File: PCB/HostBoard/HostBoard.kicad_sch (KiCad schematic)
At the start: 8 parts, among them J1 Conn_01x06, J2 Conn_01x06, J3 Conn_01x06, U1 MCP23017_SS, U2 TB6612FNG

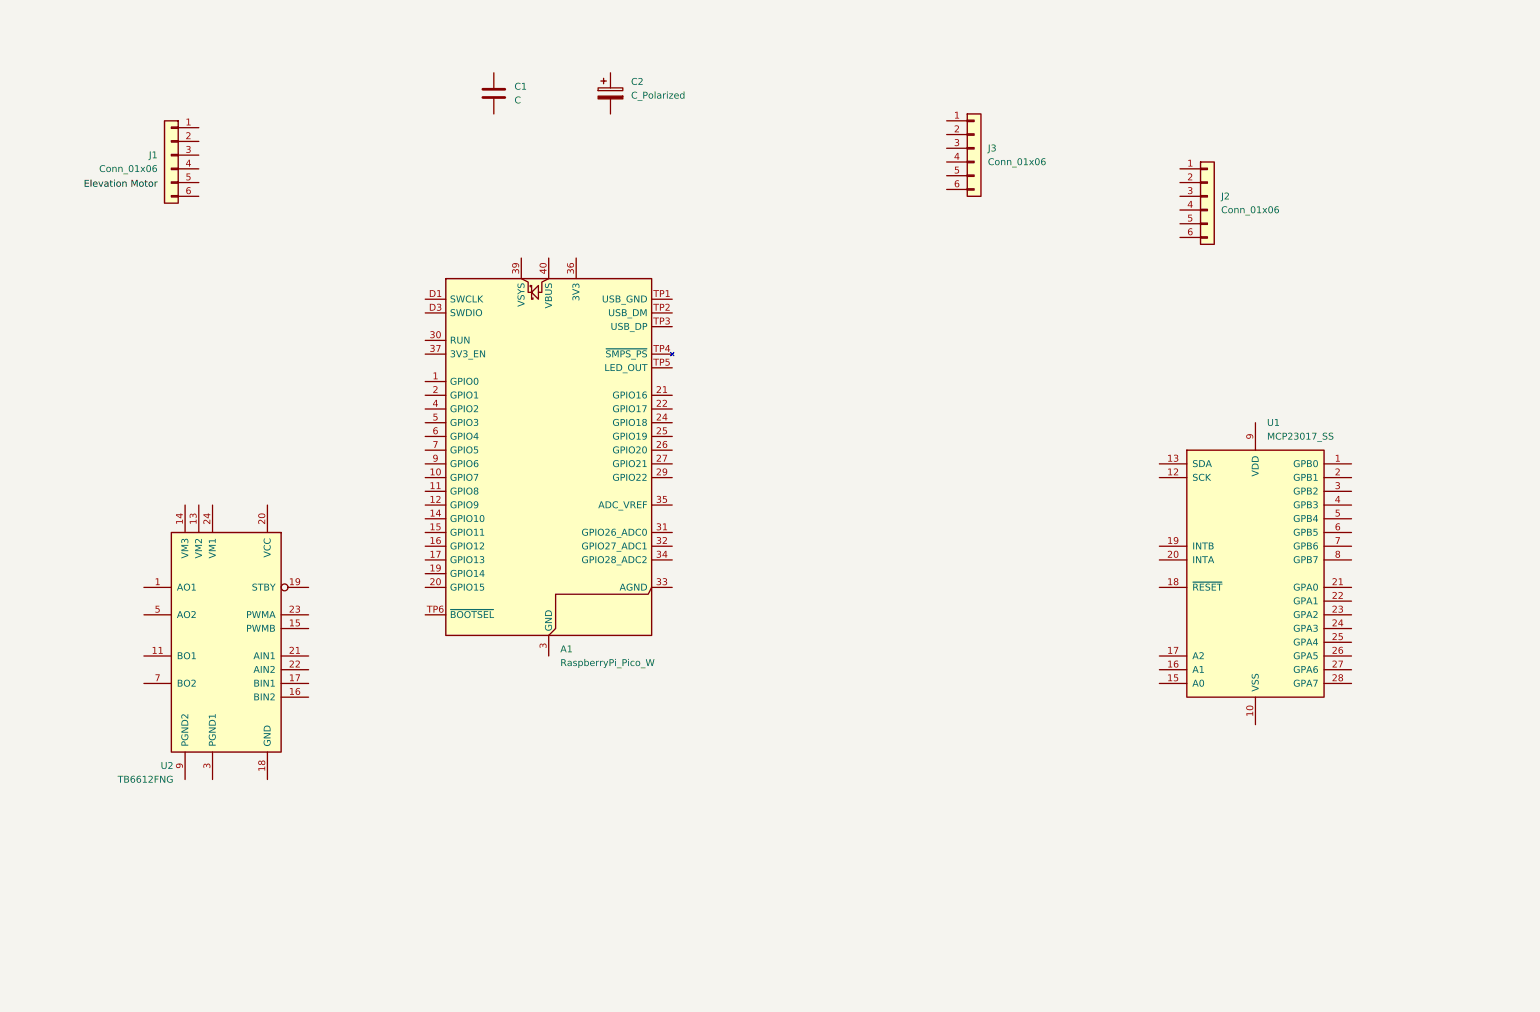
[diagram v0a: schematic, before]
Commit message: Add routing and second motor controller for automatic compass calibration. Without ability to multistep, not adding connectors for dual-use stepper motor / DC motor option.
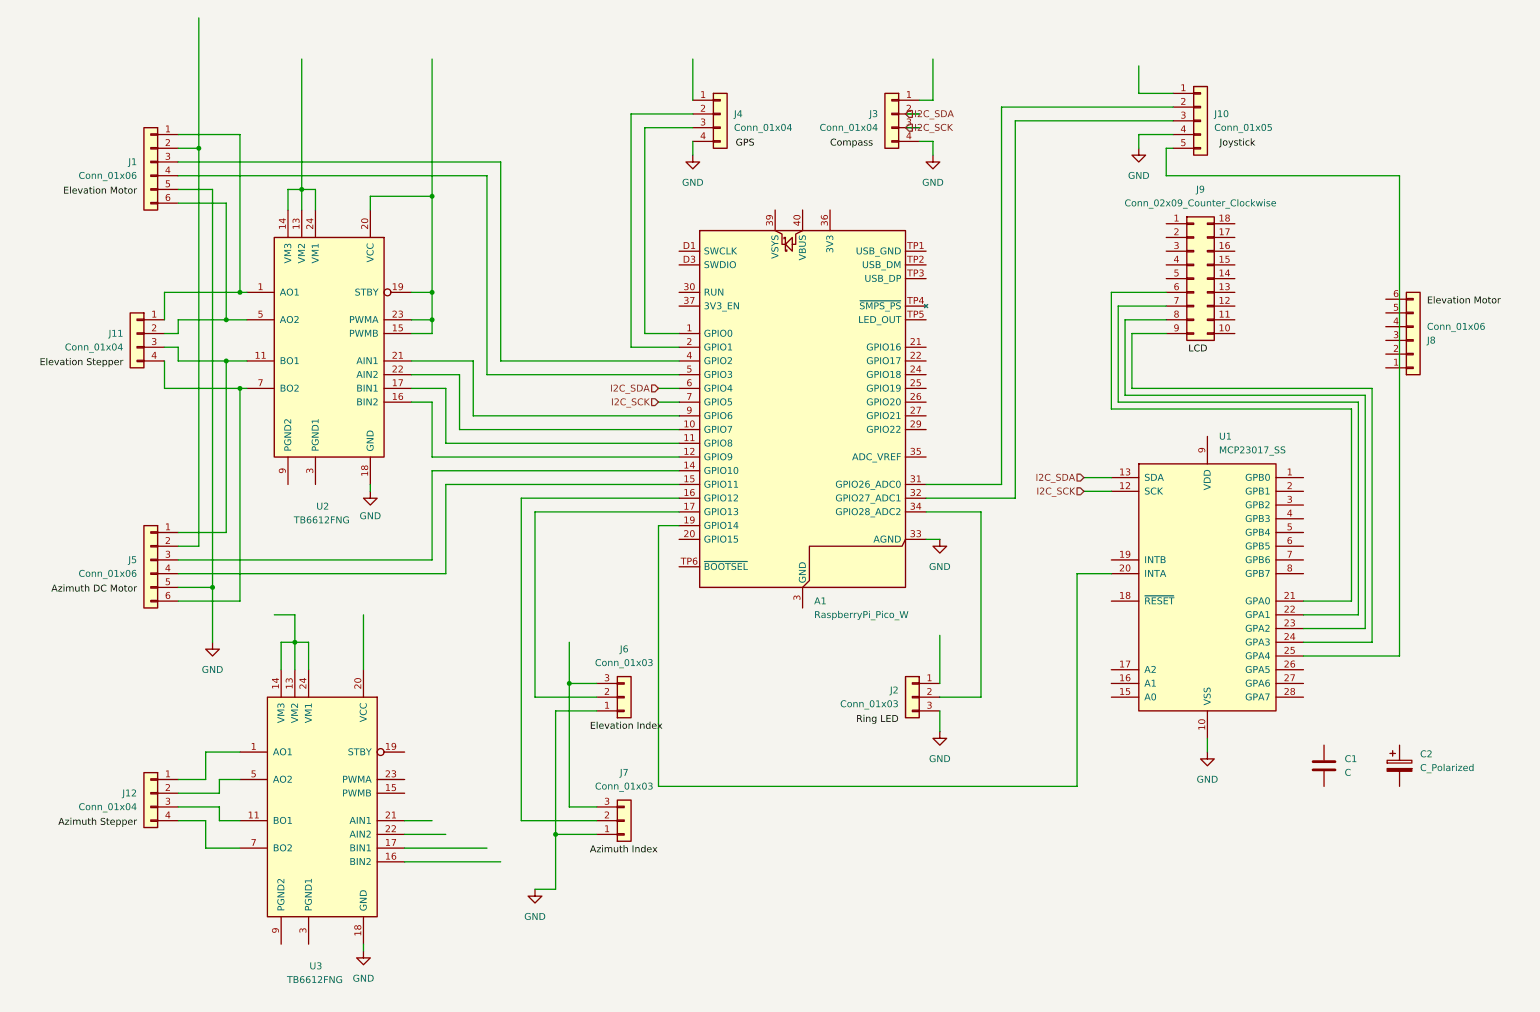
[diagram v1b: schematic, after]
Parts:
- removed J2, J3: Conn_01x06, symbol Connector_Generic:Conn_01x06
- added J10: Conn_01x05, symbol Connector_Generic:Conn_01x05
- added J11, J12, J3, J4: Conn_01x04, symbol Connector_Generic:Conn_01x04
- added J2, J6, J7: Conn_01x03, symbol Connector_Generic:Conn_01x03
- added J5, J8: Conn_01x06, symbol Connector_Generic:Conn_01x06
- added J9: Conn_02x09_Counter_Clockwise, symbol Connector_Generic:Conn_02x09_Counter_Clockwise
- added U3: TB6612FNG, Package_SO:SSOP-24_5.3x8.2mm_P0.65mm, symbol Driver_Motor:TB6612FNG
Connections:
- net at U2.1 (AO1), U2.2 (AO1): now also J1.1 (Pin_1), J11.1 (Pin_1)
- net at U2.11 (BO1), U2.12 (BO1): now also J11.3 (Pin_3), J5.1 (Pin_1)
- net at U2.13 (VM2): now also U2.14 (VM3), U2.24 (VM1)
- net at U2.15 (PWMB): now also U2.19 (STBY), U2.20 (VCC), U2.23 (PWMA)
- net at U2.16 (BIN2): now also A1.12 (GPIO9)
- net at U2.17 (BIN1): now also A1.11 (GPIO8)
- net GND: now reaches U2.18 (GND)
- net GND: now also A1.33 (AGND), J1.5 (Pin_5), U1.10 (VSS), J10.4 (Pin_4), J2.3 (Pin_3), J3.4 (Pin_4), J4.4 (Pin_4), J5.5 (Pin_5), J6.1 (Pin_1), J7.1 (Pin_1), U3.18 (GND)
- net at U2.21 (AIN1): now also A1.9 (GPIO6)
- net at U2.22 (AIN2): now also A1.10 (GPIO7)
- net at U2.5 (AO2), U2.6 (AO2): now also J1.6 (Pin_6), J11.2 (Pin_2)
- net at U2.7 (BO2), U2.8 (BO2): now also J11.4 (Pin_4), J5.6 (Pin_6)
- net at A1.1 (GPIO0): now also J4.3 (Pin_3)
- net at A1.14 (GPIO10): now also J5.3 (Pin_3)
- net at A1.15 (GPIO11): now also J5.4 (Pin_4)
- net at A1.16 (GPIO12): now also J7.2 (Pin_2)
- net at A1.17 (GPIO13): now also J6.2 (Pin_2)
- net at A1.19 (GPIO14): now also U1.20 (INTA)
- net at A1.2 (GPIO1): now also J4.2 (Pin_2)
- net at A1.31 (GPIO26_ADC0): now also J10.2 (Pin_2)
- net at A1.32 (GPIO27_ADC1): now also J10.3 (Pin_3)
- net at A1.34 (GPIO28_ADC2): now also J2.2 (Pin_2)
- net at A1.4 (GPIO2): now also J1.3 (Pin_3)
- net at A1.5 (GPIO3): now also J1.4 (Pin_4)
- net I2C_SDA: now reaches A1.6 (GPIO4)
- net I2C_SDA: now also U1.13 (SDA), J3.2 (Pin_2)
- net I2C_SCK: now reaches A1.7 (GPIO5)
- net I2C_SCK: now also U1.12 (SCK), J3.3 (Pin_3)
- net at J1.2 (Pin_2): now also J5.2 (Pin_2)
- net at U1.21 (GPA0): now also J9.6 (Pin_6)
- net at U1.22 (GPA1): now also J9.7 (Pin_7)
- net at U1.23 (GPA2): now also J9.8 (Pin_8)
- net at U1.24 (GPA3): now also J9.9 (Pin_9)
- net at U1.25 (GPA4): now also J10.5 (Pin_5)
- new net: J12.1 (Pin_1), U3.1 (AO1), U3.2 (AO1)
- new net: U3.10 (PGND2), U3.9 (PGND2)
- new net: J12.3 (Pin_3), U3.11 (BO1), U3.12 (BO1)
- new net: U3.13 (VM2), U3.14 (VM3), U3.24 (VM1)
- new net: U3.3 (PGND1), U3.4 (PGND1)
- new net: J12.2 (Pin_2), U3.5 (AO2), U3.6 (AO2)
- new net: J12.4 (Pin_4), U3.7 (BO2), U3.8 (BO2)
- new net: J6.3 (Pin_3), J7.3 (Pin_3)
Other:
- moved on the sheet: A1, C1, C2, J1, U1, U2

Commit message: Continuing schematic entry
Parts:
- removed J11, J12: Conn_01x04, symbol Connector_Generic:Conn_01x04
- removed J9: Conn_02x09_Counter_Clockwise, symbol Connector_Generic:Conn_02x09_Counter_Clockwise
- added C3: C, symbol Device:C
- added C4: C_Polarized, symbol Device:C_Polarized
- added J9: Conn_01x14, symbol Connector_Generic:Conn_01x14
- added TP1, TP2: TestPoint, symbol Connector:TestPoint
- J1: Destination (none) -> Elevation Motor
- J10: Destination (none) -> Joystick
- J2: Destination (none) -> Ring LED
- J3: Destination (none) -> Compass
- J4: Destination (none) -> GPS
- J5: Destination (none) -> Azimuth DC Motor
- J6: Destination (none) -> Elevation Index
- J7: Destination (none) -> Azimuth Index
- J8: Destination (none) -> Compass DC Motor
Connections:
- net GND: now also A1.13 (GND), A1.18 (GND), A1.23 (GND), A1.28 (GND), A1.3 (GND), A1.38 (GND), A1.8 (GND), A1.D2 (GND), C1.2, C2.2, J8.5 (Pin_5), C3.2, C4.2, J9.5 (Pin_5)
- net at U3.1 (AO1), U3.2 (AO1): now also J8.1 (Pin_1)
- net at U3.11 (BO1), U3.12 (BO1): now also TP1.1
- net Vmotor: now reaches U3.13 (VM2), U3.14 (VM3), U3.24 (VM1)
- net Vmotor: now also U2.13 (VM2), U2.14 (VM3), U2.24 (VM1)
- net +3.3V: now reaches U3.15 (PWMB)
- net +3.3V: now also A1.36 (3V3), C1.1, C2.1, J1.2 (Pin_2), J10.1 (Pin_1), J3.1 (Pin_1), J4.1 (Pin_1), J5.2 (Pin_2), J6.3 (Pin_3), J7.3 (Pin_3), J8.2 (Pin_2), U1.9 (VDD), U2.15 (PWMB), U2.19 (STBY), U2.20 (VCC), U2.23 (PWMA), U3.19 (STBY), U3.20 (VCC), U3.23 (PWMA), C3.1, C4.1, J9.1 (Pin_1)
- net at U3.16 (BIN2): now also U1.1 (GPB0)
- net at U3.17 (BIN1): now also U1.2 (GPB1)
- net at U3.21 (AIN1): now also U1.4 (GPB3)
- net at U3.22 (AIN2): now also U1.3 (GPB2)
- net at U3.5 (AO2), U3.6 (AO2): now also J8.6 (Pin_6)
- net at U3.7 (BO2), U3.8 (BO2): now also TP2.1
- net C1: now reaches J8.3 (Pin_3)
- net C1: now also U1.5 (GPB4)
- net C2: now reaches J8.4 (Pin_4)
- net C2: now also U1.6 (GPB5)
- net at U1.21 (GPA0): now also J9.6 (Pin_6)
- net at U1.22 (GPA1): now also J9.7 (Pin_7)
- net at U1.23 (GPA2): now also J9.8 (Pin_8)
- net at U1.24 (GPA3): now also J9.9 (Pin_9)
- net at A1.21 (GPIO16): now also J9.11 (Pin_11)
- net at A1.22 (GPIO17): now also J9.14 (Pin_14)
- net at A1.24 (GPIO18): now also J9.13 (Pin_13)
- net at A1.25 (GPIO19): now also J9.10 (Pin_10)
- net +5V: now reaches J2.1 (Pin_1)
- net +5V: now also J9.2 (Pin_2)
- net I2C_SCK renamed SCL_0
- net SCL_0: now also J9.4 (Pin_4)
- net I2C_SDA renamed SDA_0
- net SDA_0: now also J9.3 (Pin_3)
- no-connect marks 0 -> 9
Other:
- moved on the sheet: C1, C2, J1, J10, J2, J5, J6, J7, J8, U1, U3

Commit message: Cleanup and reorganization
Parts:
- added J11: Screw_Terminal_01x02, symbol Connector:Screw_Terminal_01x02
- J5: Destination Azimuth DC Motor -> Azimuth Motor
- J8: Destination Compass DC Motor -> Compass Motor
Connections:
- net +5V: now also A1.40 (VBUS)
- net GND: now also U1.15 (A0), U1.16 (A1), U1.17 (A2), U2.10 (PGND2), U2.3 (PGND1), U2.4 (PGND1), U2.9 (PGND2), U3.10 (PGND2), U3.3 (PGND1), U3.4 (PGND1), U3.9 (PGND2), J11.2 (Pin_2)
- net Vmotor: now also J11.1 (Pin_1)
- no-connect marks 9 -> 13
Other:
- moved on the sheet: A1, C1, C2, C3, C4, J1, J2, J3, J4, J5, J6, J7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

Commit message: Footprints assigned. Start PCB layout. Need to finish tentative schematics pin assignments
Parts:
- removed J9: Conn_01x14, symbol Connector_Generic:Conn_01x14
- added J12: Conn_02x07_Odd_Even, Connector_PinHeader_2.54mm:PinHeader_2x07_P2.54mm_Vertical, symbol Connector_Generic:Conn_02x07_Odd_Even
- A1: footprint Module:RaspberryPi_Pico_W_SMD -> Module:RaspberryPi_Pico_Common_Unspecified
- C1, C2, C3, C4: footprint (none) -> Capacitor_SMD:C_0805_2012Metric_Pad1.18x1.45mm_HandSolder
- J1: footprint (none) -> Connector_JST:JST_EH_S6B-EH_1x06_P2.50mm_Horizontal
- J10: footprint (none) -> Connector_JST:JST_EH_S5B-EH_1x05_P2.50mm_Horizontal
- J11: footprint (none) -> TerminalBlock:TerminalBlock_Xinya_XY308-2.54-2P_1x02_P2.54mm_Horizontal
- J2: renamed from J6; footprint (none) -> Connector_JST:JST_EH_S3B-EH_1x03_P2.50mm_Horizontal
- J3: renamed from J5; footprint (none) -> Connector_JST:JST_EH_S6B-EH_1x06_P2.50mm_Horizontal
- J4: renamed from J7; footprint (none) -> Connector_JST:JST_EH_S3B-EH_1x03_P2.50mm_Horizontal
- J5: renamed from J8; footprint (none) -> Connector_JST:JST_EH_S6B-EH_1x06_P2.50mm_Horizontal
- J6: renamed from J3; footprint (none) -> Connector_JST:JST_EH_S4B-EH_1x04_P2.50mm_Horizontal
- J7: renamed from J4; footprint (none) -> Connector_JST:JST_EH_S4B-EH_1x04_P2.50mm_Horizontal
- J8: renamed from J2; footprint (none) -> Connector_JST:JST_EH_S3B-EH_1x03_P2.50mm_Horizontal
- TP1, TP2: footprint (none) -> TestPoint:TestPoint_THTPad_2.5x2.5mm_Drill1.2mm
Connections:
- net +3.3V: now also J12.1 (Pin_1)
- net +5V: now also J12.2 (Pin_2)
- net GND: now also J12.5 (Pin_5)
- net SCL_0: now also J12.4 (Pin_4)
- net SDA_0: now also J12.3 (Pin_3)
- net at A1.25 (GPIO19): now also J12.10 (Pin_10)
- net at A1.21 (GPIO16): now also J12.11 (Pin_11)
- net at A1.24 (GPIO18): now also J12.13 (Pin_13)
- net at A1.22 (GPIO17): now also J12.14 (Pin_14)
- net at U1.21 (GPA0): now also J12.6 (Pin_6)
- net at U1.22 (GPA1): now also J12.7 (Pin_7)
- net at U1.23 (GPA2): now also J12.8 (Pin_8)
- net at U1.24 (GPA3): now also J12.9 (Pin_9)

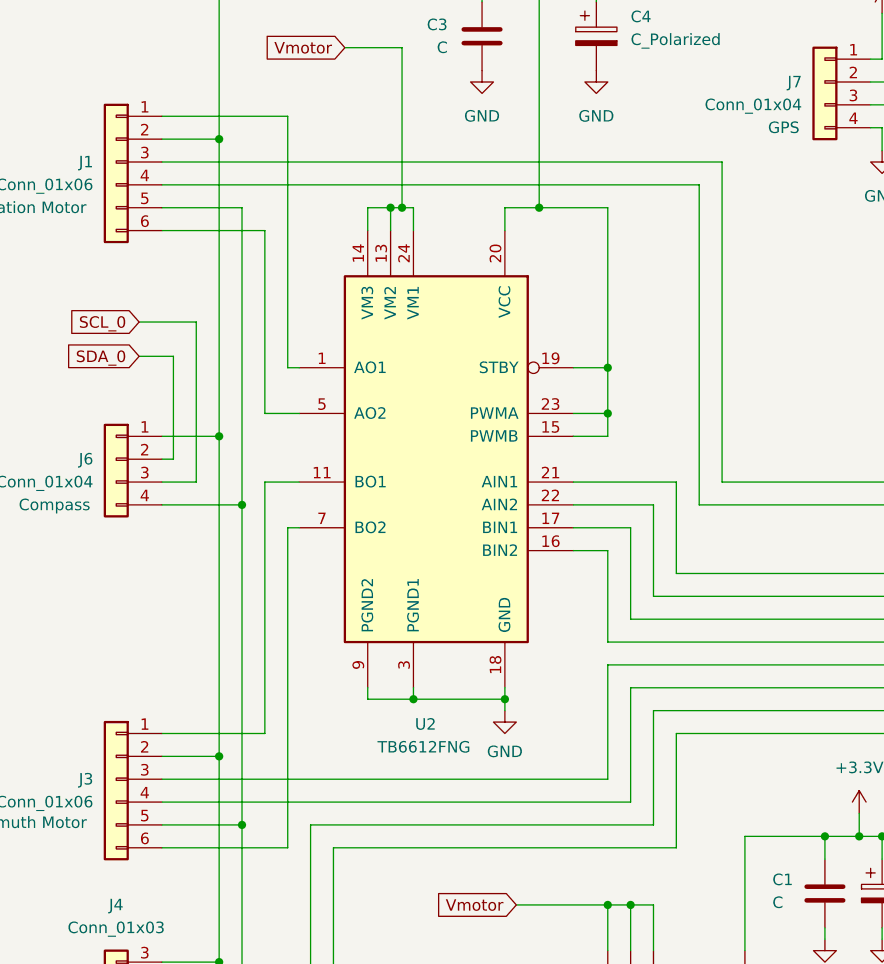
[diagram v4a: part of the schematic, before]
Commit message: PCB Routing. Signals done except VMot and TPx. Need power planes, silk and outline
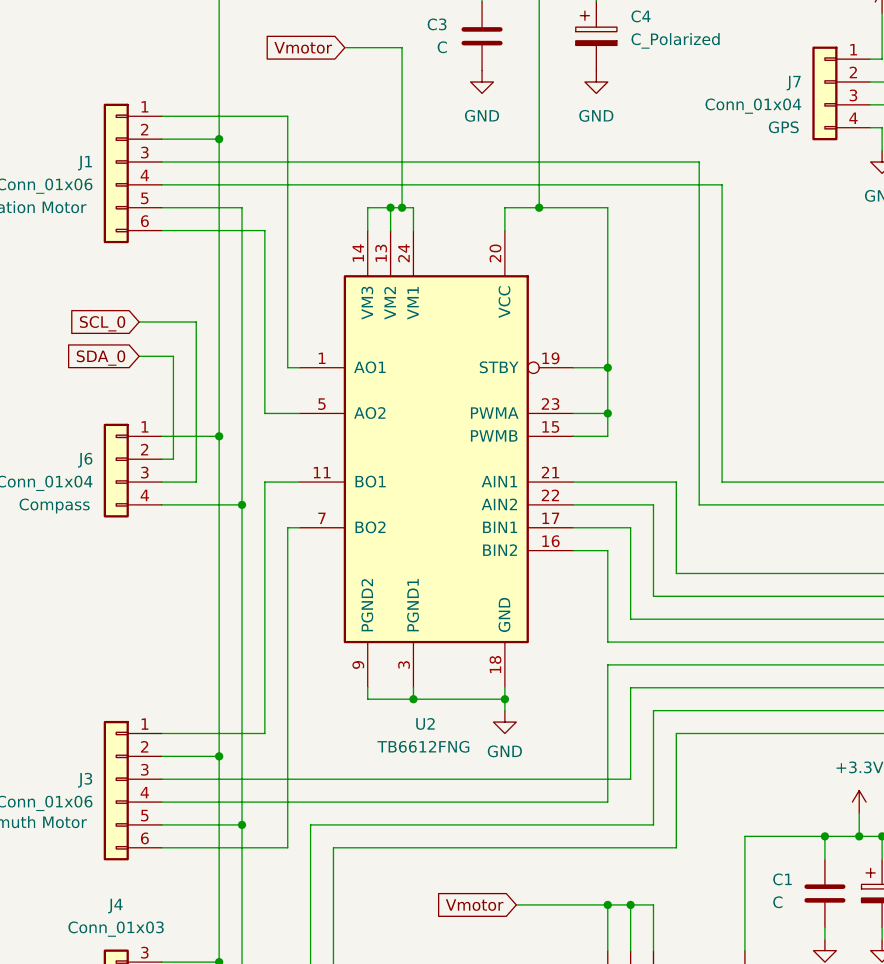
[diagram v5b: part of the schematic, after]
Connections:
- net at J3.3 (Pin_3): now also A1.15 (GPIO11); no longer A1.14 (GPIO10)
- net at J3.4 (Pin_4): now also A1.14 (GPIO10); no longer A1.15 (GPIO11)
- net at A1.4 (GPIO2): now also J1.4 (Pin_4); no longer J1.3 (Pin_3)
- net at A1.5 (GPIO3): now also J1.3 (Pin_3); no longer J1.4 (Pin_4)
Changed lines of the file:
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@@
-	(wire
-		(pts
-			(xy 88.9 114.3) (xy 36.83 114.3)
-		)
-		(stroke
-			(width 0)
-			(type default)
-		)
-	)
 	(wire
 		(pts
@@
 	(wire
 		(pts
+			(xy 96.52 43.18) (xy 96.52 81.28)
+		)
+		(stroke
+			(width 0)
+			(type default)
+		)
+	)
+	(wire
+		(pts
 			(xy 72.39 22.86) (xy 72.39 25.4)
 		)
@@
 	(wire
 		(pts
+			(xy 86.36 99.06) (xy 86.36 114.3)
+		)
+		(stroke
+			(width 0)
+			(type default)
+		)
+	)
+	(wire
+		(pts
 			(xy 45.72 175.26) (xy 36.83 175.26)
 		)
@@
 	(wire
 		(pts
+			(xy 99.06 45.72) (xy 99.06 78.74)
+		)
+		(stroke
+			(width 0)
+			(type default)
+		)
+	)
+	(wire
+		(pts
 			(xy 132.08 36.83) (xy 115.57 36.83)
 		)
@@
 	(wire
 		(pts
-			(xy 36.83 111.76) (xy 86.36 111.76)
+			(xy 36.83 111.76) (xy 88.9 111.76)
 		)
 		(stroke
@@
 	(wire
 		(pts
+			(xy 88.9 101.6) (xy 88.9 111.76)
+		)
+		(stroke
+			(width 0)
+			(type default)
+		)
+	)
+	(wire
+		(pts
 			(xy 134.62 101.6) (xy 88.9 101.6)
 		)
@@
 	(wire
 		(pts
+			(xy 36.83 45.72) (xy 99.06 45.72)
+		)
+		(stroke
+			(width 0)
+			(type default)
+		)
+	)
+	(wire
+		(pts
 			(xy 74.93 22.86) (xy 74.93 20.32)
 		)
@@
 	(wire
 		(pts
-			(xy 86.36 111.76) (xy 86.36 99.06)
-		)
-		(stroke
-			(width 0)
-			(type default)
-		)
-	)
-	(wire
-		(pts
 			(xy 124.46 151.13) (xy 124.46 153.67)
 		)
@@
 	(wire
 		(pts
-			(xy 88.9 101.6) (xy 88.9 114.3)
-		)
-		(stroke
-			(width 0)
-			(type default)
-		)
-	)
-	(wire
-		(pts
 			(xy 48.26 71.12) (xy 52.07 71.12)
 		)
@@
 	(wire
 		(pts
+			(xy 86.36 114.3) (xy 36.83 114.3)
+		)
+		(stroke
+			(width 0)
+			(type default)
+		)
+	)
+	(wire
+		(pts
 			(xy 278.13 161.29) (xy 148.59 161.29)
 		)
@@
 	(wire
 		(pts
-			(xy 96.52 45.72) (xy 36.83 45.72)
-		)
-		(stroke
-			(width 0)
-			(type default)
-		)
-	)
-	(wire
-		(pts
 			(xy 109.22 146.05) (xy 124.46 146.05)
 		)
@@
 	(wire
 		(pts
-			(xy 36.83 43.18) (xy 99.06 43.18)
-		)
-		(stroke
-			(width 0)
-			(type default)
-		)
-	)
-	(wire
-		(pts
 			(xy 85.09 25.4) (xy 85.09 22.86)
 		)
@@
 	(wire
 		(pts
-			(xy 99.06 78.74) (xy 99.06 43.18)
-		)
-		(stroke
-			(width 0)
-			(type default)
-		)
-	)
-	(wire
-		(pts
 			(xy 195.58 101.6) (xy 180.34 101.6)
 		)
@@
 	(wire
 		(pts
+			(xy 96.52 43.18) (xy 36.83 43.18)
+		)
+		(stroke
+			(width 0)
+			(type default)
+		)
+	)
+	(wire
+		(pts
 			(xy 93.98 106.68) (xy 134.62 106.68)
 		)
@@
 		)
 		(stroke
-			(width 0)
-			(type default)
-		)
-	)
-	(wire
-		(pts
-			(xy 96.52 81.28) (xy 96.52 45.72)
-		)
-		(stroke
